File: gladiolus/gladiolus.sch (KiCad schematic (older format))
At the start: 138 parts, among them J1 NEIGHBOR1, J2 NEIGHBOR2, J3 Conn_01x02_Female, J7 BONUS_ROW, Q1 Q_NPN_BEC, U1 THS4520RGT, U2 AD8330ARQZ, U3 AD9283, U4 AD9704, U5 LMH6643, U6 74LVC1G3157, U7 74LVC1G3157

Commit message: Corrected component value/manufacturer/part number for C28
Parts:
- C28: Description CAP CER 15PF 50V NP0 0402 -> CAP CER 10000PF 50V X7R 0603; Manufacturer Murata -> Samsung Electro-Mechanics; Part Number GRM1555C1H150GA01D -> CL10B103KB8NFNC
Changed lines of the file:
@@
 F 2 "gsg-modules:0603" H 1938 2500 50  0001 C CNN
 F 3 "" H 1900 2650 50  0000 C CNN
-F 4 "Murata" H 1900 2650 60  0001 C CNN "Manufacturer"
-F 5 "GRM1555C1H150GA01D" H 1900 2650 60  0001 C CNN "Part Number"
-F 6 "CAP CER 15PF 50V NP0 0402" H 1900 2650 60  0001 C CNN "Description"
+F 4 "Samsung Electro-Mechanics" H 1900 2650 60  0001 C CNN "Manufacturer"
+F 5 "CL10B103KB8NFNC" H 1900 2650 60  0001 C CNN "Part Number"
+F 6 "CAP CER 10000PF 50V X7R 0603 " H 1900 2650 60  0001 C CNN "Description"
 	1    1900 2650
 	0    -1   -1   0

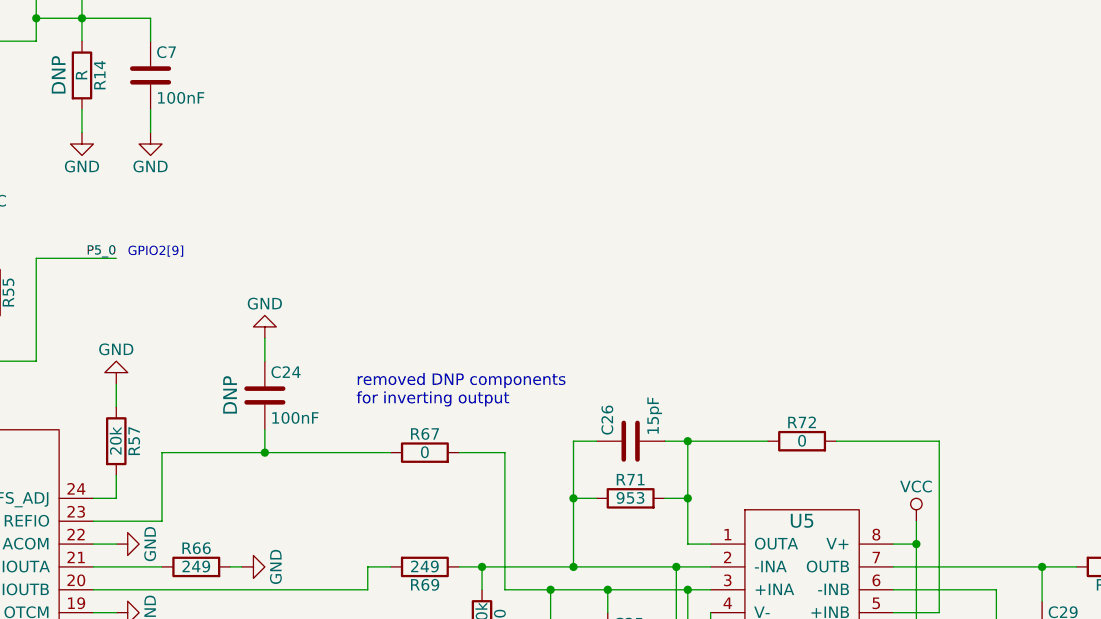
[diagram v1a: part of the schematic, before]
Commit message: Changed switch to turn off TX while the DAC is in sleep mode.
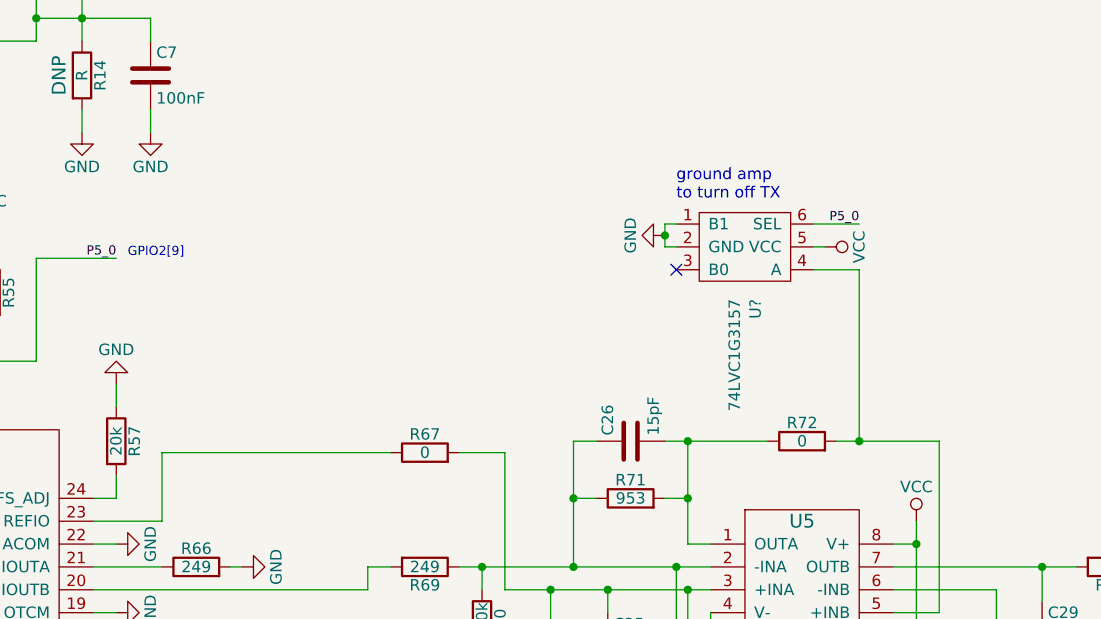
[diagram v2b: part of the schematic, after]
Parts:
- removed C24: 100nF, gsg-modules:0603, symbol Device:C
- added U?: 74LVC1G3157, gsg-modules:SOT363, symbol gsg-symbols:74LVC1G3157
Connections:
- net GND: now also U?.1 (B1), U?.2 (GND)
- net P5_0: now also U?.6 (SEL)
- net VCC: now also U?.5 (VCC)
- net at R72.2, U5.5 (+INB): now also U?.4 (A)
- no-connect marks 63 -> 64
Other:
- note added: "ground amp\nto turn off TX"
- note removed: "removed DNP components\nfor inverting output"
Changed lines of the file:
@@
-$EndComp
-$Comp
-L Device:C C24
-U 1 1 586FE5EE
-P 4600 6650
-F 0 "C24" H 4625 6750 50  0000 L CNN
-F 1 "100nF" H 4625 6550 50  0000 L CNN
-F 2 "gsg-modules:0603" H 4638 6500 50  0001 C CNN
-F 3 "" H 4600 6650 50  0000 C CNN
-F 4 "Murata" H 4600 6650 60  0001 C CNN "Manufacturer"
-F 5 "GRM188R71C104KA01D" H 4600 6650 60  0001 C CNN "Part Number"
-F 6 "CAP CER 0.1UF 16V X7R 0603" H 4600 6650 60  0001 C CNN "Description"
-F 7 "DNP" V 4450 6650 60  0000 C CNN "Note"
-	1    4600 6650
-	1    0    0    -1
-$EndComp
-$Comp
-L power:GND #PWR088
-U 1 1 586FE7EA
-P 4600 6400
-F 0 "#PWR088" H 4600 6150 50  0001 C CNN
-F 1 "GND" H 4600 6250 50  0000 C CNN
-F 2 "" H 4600 6400 50  0000 C CNN
-F 3 "" H 4600 6400 50  0000 C CNN
-	1    4600 6400
-	-1   0    0    1
 $EndComp
 $Comp
@@
 Wire Wire Line
 	4150 7200 3850 7200
-Wire Wire Line
-	4150 6900 4600 6900
-Wire Wire Line
-	4600 6900 4600 6800
-Connection ~ 4600 6900
-Wire Wire Line
-	4600 6500 4600 6400
 Connection ~ 8850 8000
 Wire Wire Line
-	7100 6850 7550 6850
+	7100 6850 7200 6850
 Wire Wire Line
 	8450 8000 8850 8000
@@
 Text Notes 6600 8350 0    50   ~ 0
 short +/- inputs\nto turn off TX
-Text Notes 5000 6700 0    50   ~ 0
-removed DNP components\nfor inverting output
 $Comp
 L Device:C C29
@@
 Wire Wire Line
 	4450 7400 4500 7400
-Wire Wire Line
-	4600 6900 5150 6900
 Wire Wire Line
 	5550 7400 5950 7400
@@
 Wire Wire Line
 	15800 3450 16100 3450
+Text Notes 6400 5800 0    50   ~ 0
+ground amp\nto turn off TX
+$Comp
+L gsg-symbols:74LVC1G3157 U?
+U 1 1 5CB72BB9
+P 6700 6000
+F 0 "U?" V 6746 5772 50  0000 R CNN
+F 1 "74LVC1G3157" V 6655 5772 50  0000 R CNN
+F 2 "gsg-modules:SOT363" H 6700 6000 50  0001 C CNN
+F 3 "" H 6700 6000 50  0001 C CNN
+F 4 "Diodes Incorporated" V 6655 5772 50  0001 R CNN "Manufacturer"
+F 5 "74LVC1G3157DW-7" H 6700 6000 50  0001 C CNN "Part Number"
+F 6 "IC SWITCH SPDT 6 OHM SOT363" V 6564 5772 50  0001 R CNN "Description"
+	1    6700 6000
+	1    0    0    -1
+$EndComp
+$Comp
+L power:VCC #PWR?
+U 1 1 5CB72BC0
+P 7050 6000
+F 0 "#PWR?" H 7050 5850 50  0001 C CNN
+F 1 "VCC" H 7050 6150 50  0000 C CNN
+F 2 "" H 7050 6000 60  0000 C CNN
+F 3 "" H 7050 6000 60  0000 C CNN
+	1    7050 6000
+	0    1    1    0
+$EndComp
+Wire Wire Line
+	7000 6000 7050 6000
+$Comp
+L power:GND #PWR?
+U 1 1 5CB72BC7
+P 6350 5950
+F 0 "#PWR?" H 6350 5700 50  0001 C CNN
+F 1 "GND" H 6350 5800 50  0000 C CNN
+F 2 "" H 6350 5950 50  0000 C CNN
+F 3 "" H 6350 5950 50  0000 C CNN
+	1    6350 5950
+	0    1    1    0
+$EndComp
+Wire Wire Line
+	6350 6000 6400 6000
+Text Label 7200 5900 2    40   ~ 0
+P5_0
+Wire Wire Line
+	7000 5900 7200 5900
+NoConn ~ 6400 6100
+Wire Wire Line
+	4150 6900 5150 6900
+Wire Wire Line
+	7000 6100 7200 6100
+Wire Wire Line
+	7200 6100 7200 6850
+Connection ~ 7200 6850
+Wire Wire Line
+	7200 6850 7550 6850
+Wire Wire Line
+	6400 5900 6350 5900
+Wire Wire Line
+	6350 5900 6350 5950
+Connection ~ 6350 5950
+Wire Wire Line
+	6350 5950 6350 6000
 $EndSCHEMATC

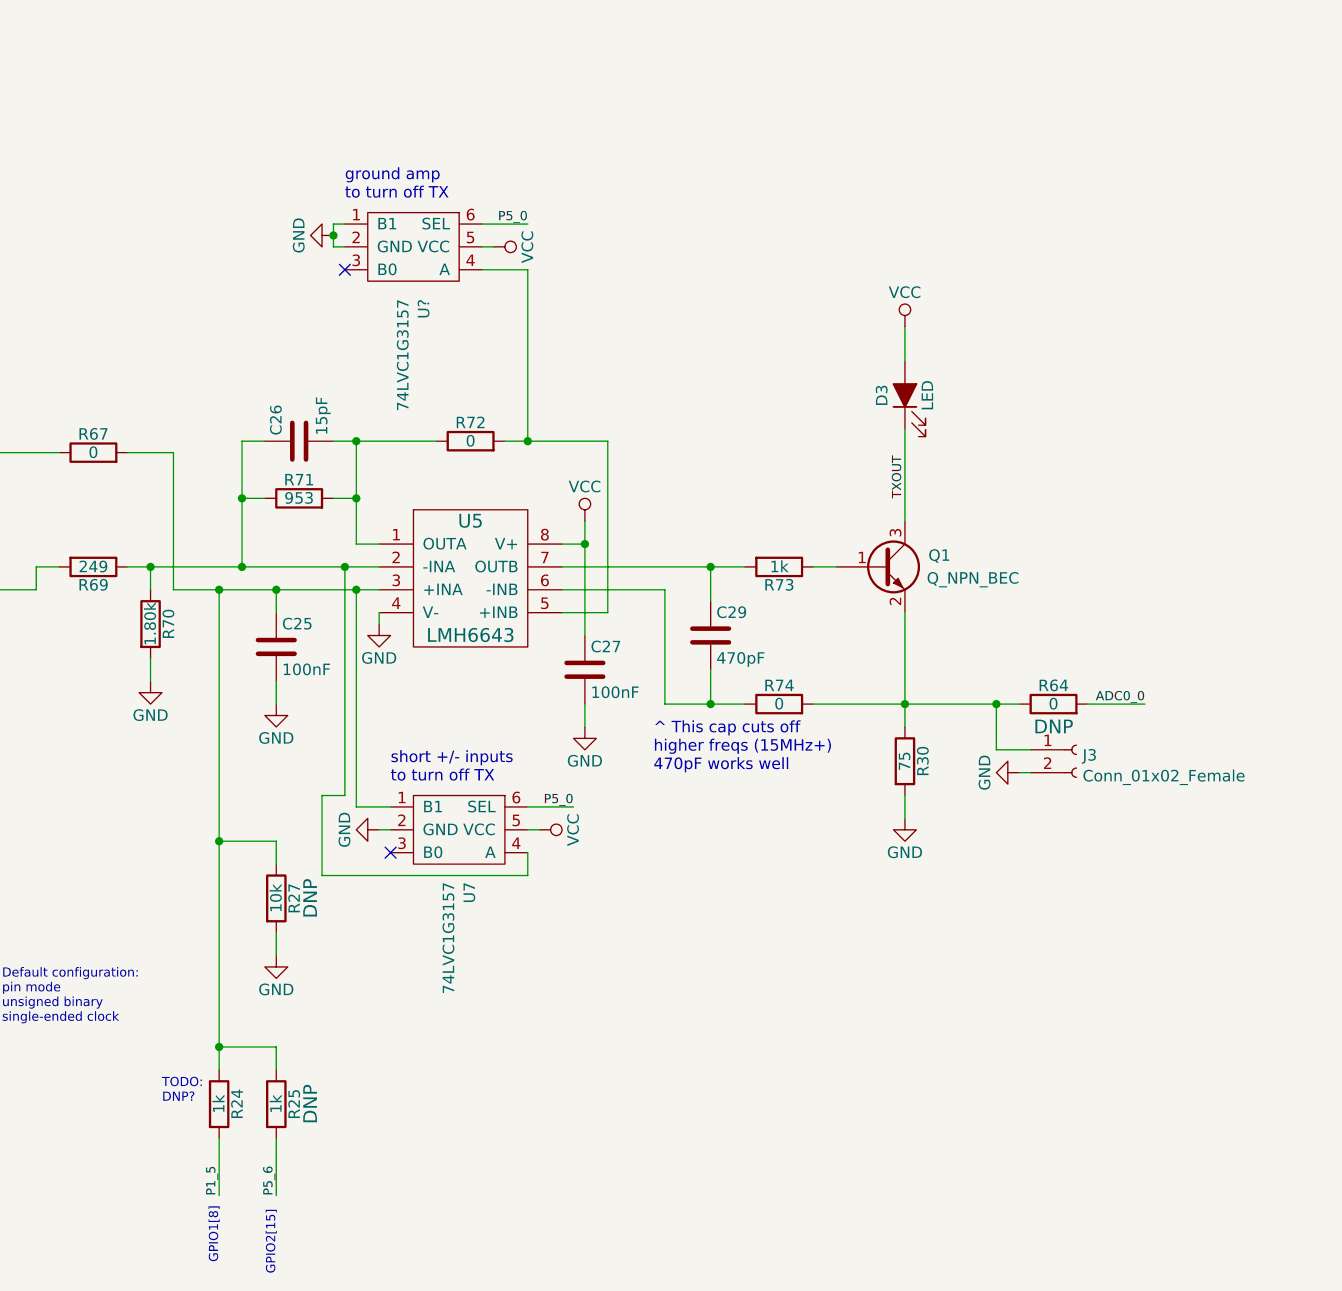
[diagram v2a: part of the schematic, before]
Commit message: Removed several DNP components
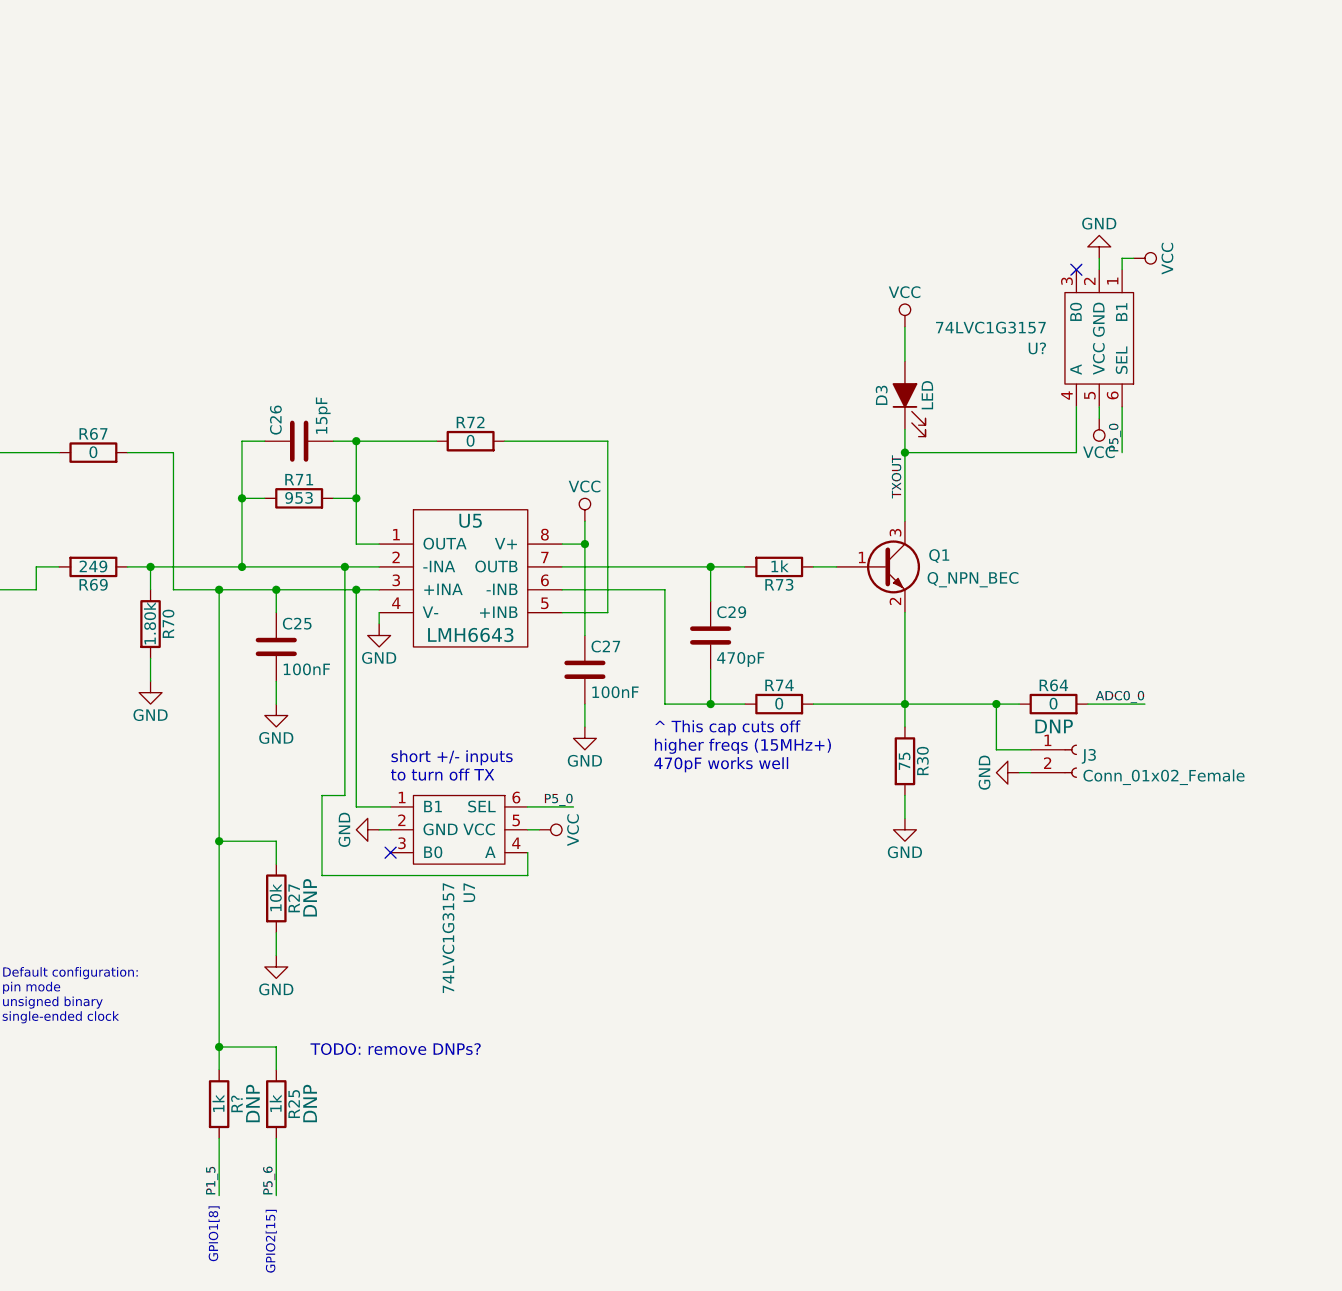
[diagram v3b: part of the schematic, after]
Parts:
- removed R24: 1k, gsg-modules:0603, symbol Device:R
- added R?: 1k, gsg-modules:0603, symbol Device:R
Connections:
- net GND: no longer U?.1 (B1)
- net P1_5: now also R?.2
- net TXOUT: now also U?.4 (A)
- net VCC: now also U?.1 (B1)
- net at C25.1, R25.1, R27.1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: now also R?.1
- net at R72.2, U5.5 (+INB): no longer U?.4 (A)
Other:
- note added: "TODO: remove DNPs?"
- note removed: "TODO:\nDNP?"
- note removed: "ground amp\nto turn off TX"
- moved on the sheet: U?
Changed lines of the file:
@@
 $EndComp
 $Comp
-L Device:R R24
-U 1 1 5849D7DD
-P 5850 9750
-F 0 "R24" V 5930 9750 50  0000 C CNN
-F 1 "1k" V 5850 9750 50  0000 C CNN
-F 2 "gsg-modules:0603" V 5780 9750 50  0001 C CNN
-F 3 "" H 5850 9750 50  0000 C CNN
-F 4 "Yageo" H 5850 9750 60  0001 C CNN "Manufacturer"
-F 5 "RC0603JR-071KL" H 5850 9750 60  0001 C CNN "Part Number"
-F 6 "RES SMD 1K OHM 5% 1/10W 0603" H 5850 9750 60  0001 C CNN "Description"
-	1    5850 9750
-	1    0    0    -1
-$EndComp
-$Comp
 L gsg-symbols:THS4520RGT U1
 U 1 1 585AF88F
@@
 Connection ~ 8850 8000
 Wire Wire Line
-	7100 6850 7200 6850
-Wire Wire Line
 	8450 8000 8850 8000
 Wire Wire Line
@@
 Text Label 1400 2800 1    50   ~ 0
 P2_1
-Text Notes 5600 9750 0    40   ~ 0
-TODO:\nDNP?
 Text Notes 6600 8350 0    50   ~ 0
 short +/- inputs\nto turn off TX
@@
 	8850 6500 8850 6350
 Wire Wire Line
-	8850 6800 8850 7200
+	8850 6800 8850 6900
 Wire Wire Line
 	15200 3450 15500 3450
 Wire Wire Line
 	15800 3450 16100 3450
-Text Notes 6400 5800 0    50   ~ 0
-ground amp\nto turn off TX
 $Comp
 L gsg-symbols:74LVC1G3157 U?
 U 1 1 5CB72BB9
-P 6700 6000
-F 0 "U?" V 6746 5772 50  0000 R CNN
-F 1 "74LVC1G3157" V 6655 5772 50  0000 R CNN
-F 2 "gsg-modules:SOT363" H 6700 6000 50  0001 C CNN
-F 3 "" H 6700 6000 50  0001 C CNN
-F 4 "Diodes Incorporated" V 6655 5772 50  0001 R CNN "Manufacturer"
-F 5 "74LVC1G3157DW-7" H 6700 6000 50  0001 C CNN "Part Number"
-F 6 "IC SWITCH SPDT 6 OHM SOT363" V 6564 5772 50  0001 R CNN "Description"
-	1    6700 6000
-	1    0    0    -1
+P 9700 6400
+F 0 "U?" V 9746 6172 50  0000 R CNN
+F 1 "74LVC1G3157" V 9655 6172 50  0000 R CNN
+F 2 "gsg-modules:SOT363" H 9700 6400 50  0001 C CNN
+F 3 "" H 9700 6400 50  0001 C CNN
+F 4 "Diodes Incorporated" V 9655 6172 50  0001 R CNN "Manufacturer"
+F 5 "74LVC1G3157DW-7" H 9700 6400 50  0001 C CNN "Part Number"
+F 6 "IC SWITCH SPDT 6 OHM SOT363" V 9564 6172 50  0001 R CNN "Description"
+	1    9700 6400
+	0    1    1    0
 $EndComp
 $Comp
 L power:VCC #PWR?
 U 1 1 5CB72BC0
-P 7050 6000
-F 0 "#PWR?" H 7050 5850 50  0001 C CNN
-F 1 "VCC" H 7050 6150 50  0000 C CNN
-F 2 "" H 7050 6000 60  0000 C CNN
-F 3 "" H 7050 6000 60  0000 C CNN
-	1    7050 6000
-	0    1    1    0
+P 9700 6750
+F 0 "#PWR?" H 9700 6600 50  0001 C CNN
+F 1 "VCC" H 9700 6900 50  0000 C CNN
+F 2 "" H 9700 6750 60  0000 C CNN
+F 3 "" H 9700 6750 60  0000 C CNN
+	1    9700 6750
+	-1   0    0    1
 $EndComp
 Wire Wire Line
-	7000 6000 7050 6000
+	9700 6700 9700 6750
 $Comp
 L power:GND #PWR?
 U 1 1 5CB72BC7
-P 6350 5950
-F 0 "#PWR?" H 6350 5700 50  0001 C CNN
-F 1 "GND" H 6350 5800 50  0000 C CNN
-F 2 "" H 6350 5950 50  0000 C CNN
-F 3 "" H 6350 5950 50  0000 C CNN
-	1    6350 5950
-	0    1    1    0
+P 9700 6050
+F 0 "#PWR?" H 9700 5800 50  0001 C CNN
+F 1 "GND" H 9700 5900 50  0000 C CNN
+F 2 "" H 9700 6050 50  0000 C CNN
+F 3 "" H 9700 6050 50  0000 C CNN
+	1    9700 6050
+	-1   0    0    1
 $EndComp
 Wire Wire Line
-	6350 6000 6400 6000
-Text Label 7200 5900 2    40   ~ 0
+	9700 6050 9700 6100
+Text Label 9800 6900 1    40   ~ 0
 P5_0
 Wire Wire Line
-	7000 5900 7200 5900
-NoConn ~ 6400 6100
+	9800 6700 9800 6900
+NoConn ~ 9600 6100
 Wire Wire Line
 	4150 6900 5150 6900
 Wire Wire Line
-	7000 6100 7200 6100
+	9600 6700 9600 6900
 Wire Wire Line
-	7200 6100 7200 6850
-Connection ~ 7200 6850
+	9600 6900 8850 6900
+$Comp
+L Device:R R?
+U 1 1 5CB7D036
+P 5850 9750
+F 0 "R?" V 5930 9750 50  0000 C CNN
+F 1 "1k" V 5850 9750 50  0000 C CNN
+F 2 "gsg-modules:0603" V 5780 9750 50  0001 C CNN
+F 3 "" H 5850 9750 50  0000 C CNN
+F 4 "Yageo" H 5850 9750 60  0001 C CNN "Manufacturer"
+F 5 "RC0603JR-071KL" H 5850 9750 60  0001 C CNN "Part Number"
+F 6 "RES SMD 1K OHM 5% 1/10W 0603" H 5850 9750 60  0001 C CNN "Description"
+F 7 "DNP" V 6000 9750 60  0000 C CNN "Note"
+	1    5850 9750
+	1    0    0    -1
+$EndComp
+Text Notes 6250 9550 0    50   ~ 0
+TODO: remove DNPs?
 Wire Wire Line
-	7200 6850 7550 6850
+	7100 6850 7550 6850
+$Comp
+L power:VCC #PWR?
+U 1 1 5CBE6FDC
+P 9850 6050
+F 0 "#PWR?" H 9850 5900 50  0001 C CNN
+F 1 "VCC" H 9850 6200 50  0000 C CNN
+F 2 "" H 9850 6050 60  0000 C CNN
+F 3 "" H 9850 6050 60  0000 C CNN
+	1    9850 6050
+	0    1    1    0
+$EndComp
 Wire Wire Line
-	6400 5900 6350 5900
+	9850 6050 9800 6050
 Wire Wire Line
-	6350 5900 6350 5950
-Connection ~ 6350 5950
+	9800 6050 9800 6100
+Connection ~ 8850 6900
 Wire Wire Line
-	6350 5950 6350 6000
+	8850 6900 8850 7200
 $EndSCHEMATC

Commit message: added notes
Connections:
- net TXOUT: no longer U?.4 (A)
- net VCC: no longer D3.2 (A)
- new net: D3.2 (A), U?.4 (A)
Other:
- note added: "add test points to\ntransistor pins"
- moved on the sheet: U?
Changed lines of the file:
@@
 $EndComp
 $Comp
-L power:VCC #PWR046
-U 1 1 58498676
-P 8850 6350
-F 0 "#PWR046" H 8850 6200 50  0001 C CNN
-F 1 "VCC" H 8850 6500 50  0000 C CNN
-F 2 "" H 8850 6350 60  0000 C CNN
-F 3 "" H 8850 6350 60  0000 C CNN
-	1    8850 6350
-	1    0    0    -1
-$EndComp
-$Comp
 L Device:Q_NPN_BEC Q1
 U 1 1 5849B3A4
@@
 	8850 6500 8850 6350
 Wire Wire Line
-	8850 6800 8850 6900
-Wire Wire Line
 	15200 3450 15500 3450
 Wire Wire Line
@@
 L gsg-symbols:74LVC1G3157 U?
 U 1 1 5CB72BB9
-P 9700 6400
-F 0 "U?" V 9746 6172 50  0000 R CNN
-F 1 "74LVC1G3157" V 9655 6172 50  0000 R CNN
-F 2 "gsg-modules:SOT363" H 9700 6400 50  0001 C CNN
-F 3 "" H 9700 6400 50  0001 C CNN
-F 4 "Diodes Incorporated" V 9655 6172 50  0001 R CNN "Manufacturer"
-F 5 "74LVC1G3157DW-7" H 9700 6400 50  0001 C CNN "Part Number"
-F 6 "IC SWITCH SPDT 6 OHM SOT363" V 9564 6172 50  0001 R CNN "Description"
-	1    9700 6400
+P 9700 5850
+F 0 "U?" V 9746 5622 50  0000 R CNN
+F 1 "74LVC1G3157" V 9655 5622 50  0000 R CNN
+F 2 "gsg-modules:SOT363" H 9700 5850 50  0001 C CNN
+F 3 "" H 9700 5850 50  0001 C CNN
+F 4 "Diodes Incorporated" V 9655 5622 50  0001 R CNN "Manufacturer"
+F 5 "74LVC1G3157DW-7" H 9700 5850 50  0001 C CNN "Part Number"
+F 6 "IC SWITCH SPDT 6 OHM SOT363" V 9564 5622 50  0001 R CNN "Description"
+	1    9700 5850
 	0    1    1    0
 $EndComp
@@
 L power:VCC #PWR?
 U 1 1 5CB72BC0
-P 9700 6750
-F 0 "#PWR?" H 9700 6600 50  0001 C CNN
-F 1 "VCC" H 9700 6900 50  0000 C CNN
-F 2 "" H 9700 6750 60  0000 C CNN
-F 3 "" H 9700 6750 60  0000 C CNN
-	1    9700 6750
+P 9700 6200
+F 0 "#PWR?" H 9700 6050 50  0001 C CNN
+F 1 "VCC" H 9700 6350 50  0000 C CNN
+F 2 "" H 9700 6200 60  0000 C CNN
+F 3 "" H 9700 6200 60  0000 C CNN
+	1    9700 6200
 	-1   0    0    1
 $EndComp
 Wire Wire Line
-	9700 6700 9700 6750
+	9700 6150 9700 6200
 $Comp
 L power:GND #PWR?
 U 1 1 5CB72BC7
-P 9700 6050
-F 0 "#PWR?" H 9700 5800 50  0001 C CNN
-F 1 "GND" H 9700 5900 50  0000 C CNN
-F 2 "" H 9700 6050 50  0000 C CNN
-F 3 "" H 9700 6050 50  0000 C CNN
-	1    9700 6050
+P 9700 5500
+F 0 "#PWR?" H 9700 5250 50  0001 C CNN
+F 1 "GND" H 9700 5350 50  0000 C CNN
+F 2 "" H 9700 5500 50  0000 C CNN
+F 3 "" H 9700 5500 50  0000 C CNN
+	1    9700 5500
 	-1   0    0    1
 $EndComp
 Wire Wire Line
-	9700 6050 9700 6100
-Text Label 9800 6900 1    40   ~ 0
+	9700 5500 9700 5550
+Text Label 9800 6350 1    40   ~ 0
 P5_0
 Wire Wire Line
-	9800 6700 9800 6900
-NoConn ~ 9600 6100
+	9800 6150 9800 6350
+NoConn ~ 9600 5550
 Wire Wire Line
 	4150 6900 5150 6900
 Wire Wire Line
-	9600 6700 9600 6900
+	9600 6150 9600 6350
 Wire Wire Line
-	9600 6900 8850 6900
+	9600 6350 8850 6350
 $Comp
 L Device:R R?
@@
 L power:VCC #PWR?
 U 1 1 5CBE6FDC
-P 9850 6050
-F 0 "#PWR?" H 9850 5900 50  0001 C CNN
-F 1 "VCC" H 9850 6200 50  0000 C CNN
-F 2 "" H 9850 6050 60  0000 C CNN
-F 3 "" H 9850 6050 60  0000 C CNN
-	1    9850 6050
+P 9850 5500
+F 0 "#PWR?" H 9850 5350 50  0001 C CNN
+F 1 "VCC" H 9850 5650 50  0000 C CNN
+F 2 "" H 9850 5500 60  0000 C CNN
+F 3 "" H 9850 5500 60  0000 C CNN
+	1    9850 5500
 	0    1    1    0
 $EndComp
 Wire Wire Line
-	9850 6050 9800 6050
+	9850 5500 9800 5500
 Wire Wire Line
-	9800 6050 9800 6100
-Connection ~ 8850 6900
+	9800 5500 9800 5550
 Wire Wire Line
-	8850 6900 8850 7200
+	8850 6800 8850 7200
+Text Notes 9100 7700 0    50   ~ 0
+add test points to\ntransistor pins
 $EndSCHEMATC
